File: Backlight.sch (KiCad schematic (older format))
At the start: 52 parts, among them Q2 Q_NMOS_GSD

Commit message: added new generic SMD pad footprints and footprint associations
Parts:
- LED13, LED14, LED15, LED16, LED17, LED18, LED19, LED20, LED21, LED22, LED23, LED24, LED25, LED26, LED27, LED28, LED29, LED30, LED31, LED32, LED33, LED34, LED35, LED36, LED37: footprint (none) -> LED_SMD:LED_0805_2012Metric
- Q2: footprint (none) -> Package_TO_SOT_SMD:SOT-23
- R12, R13, R14, R15, R16, R17, R18, R19, R20, R21, R22, R23, R24, R25, R26, R27, R28, R29, R30, R31, R32, R33, R34, R35, R36: footprint (none) -> Resistor_SMD:R_0805_2012Metric

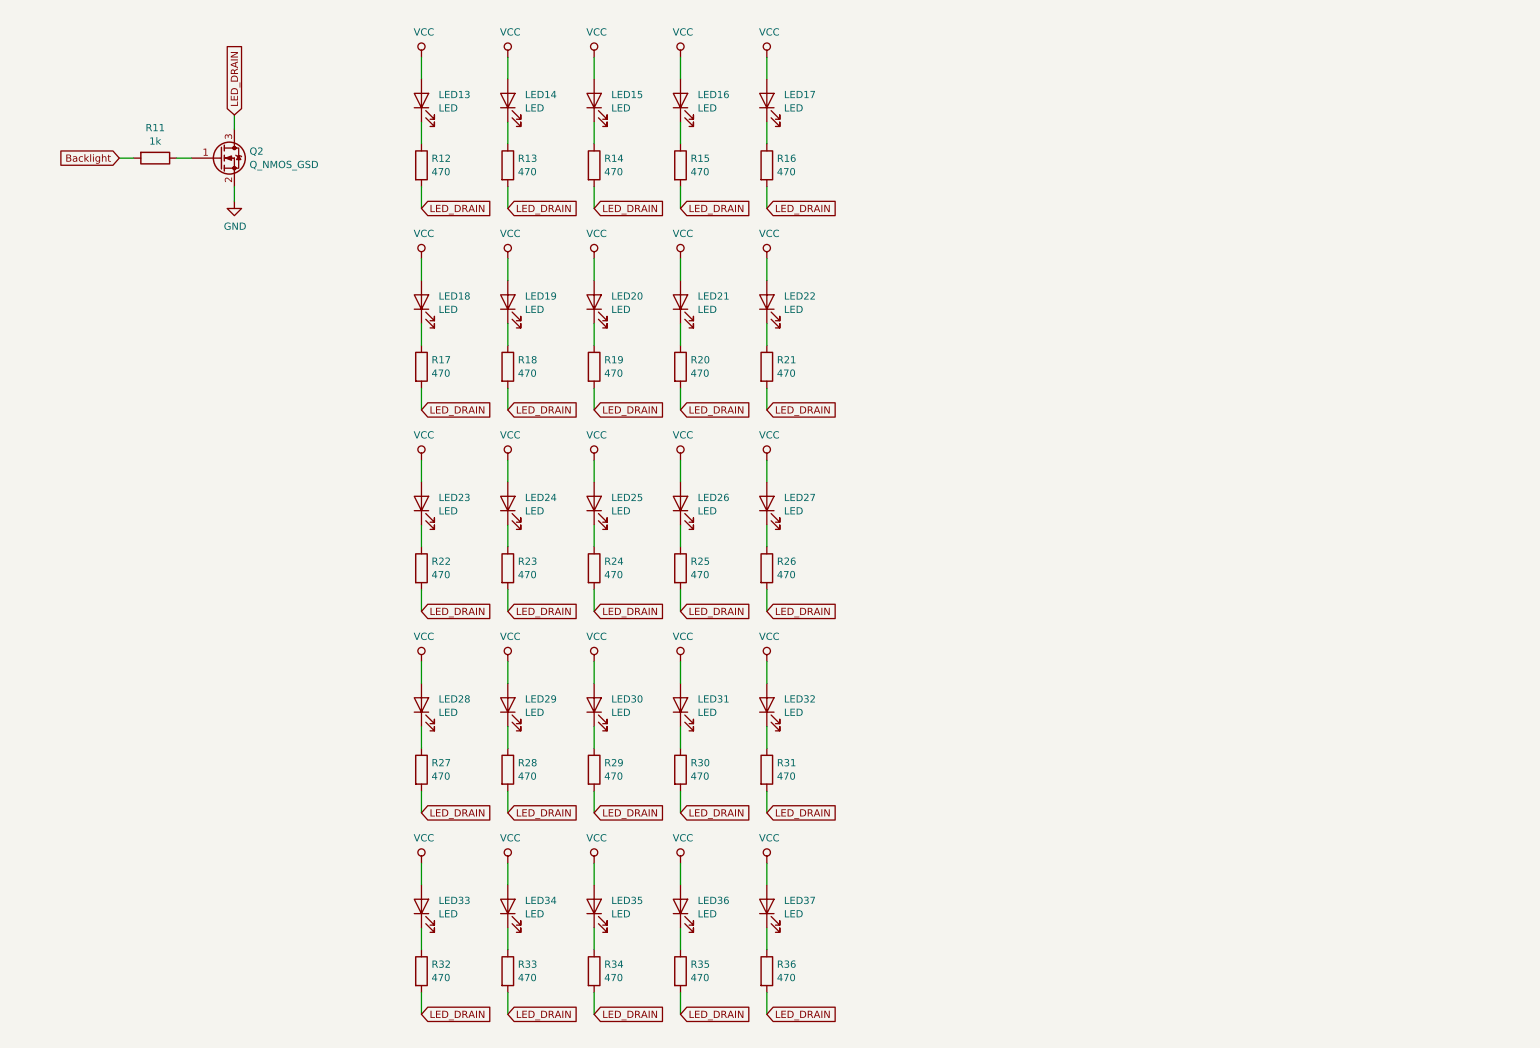
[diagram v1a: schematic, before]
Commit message: updated schematic with more backlight options
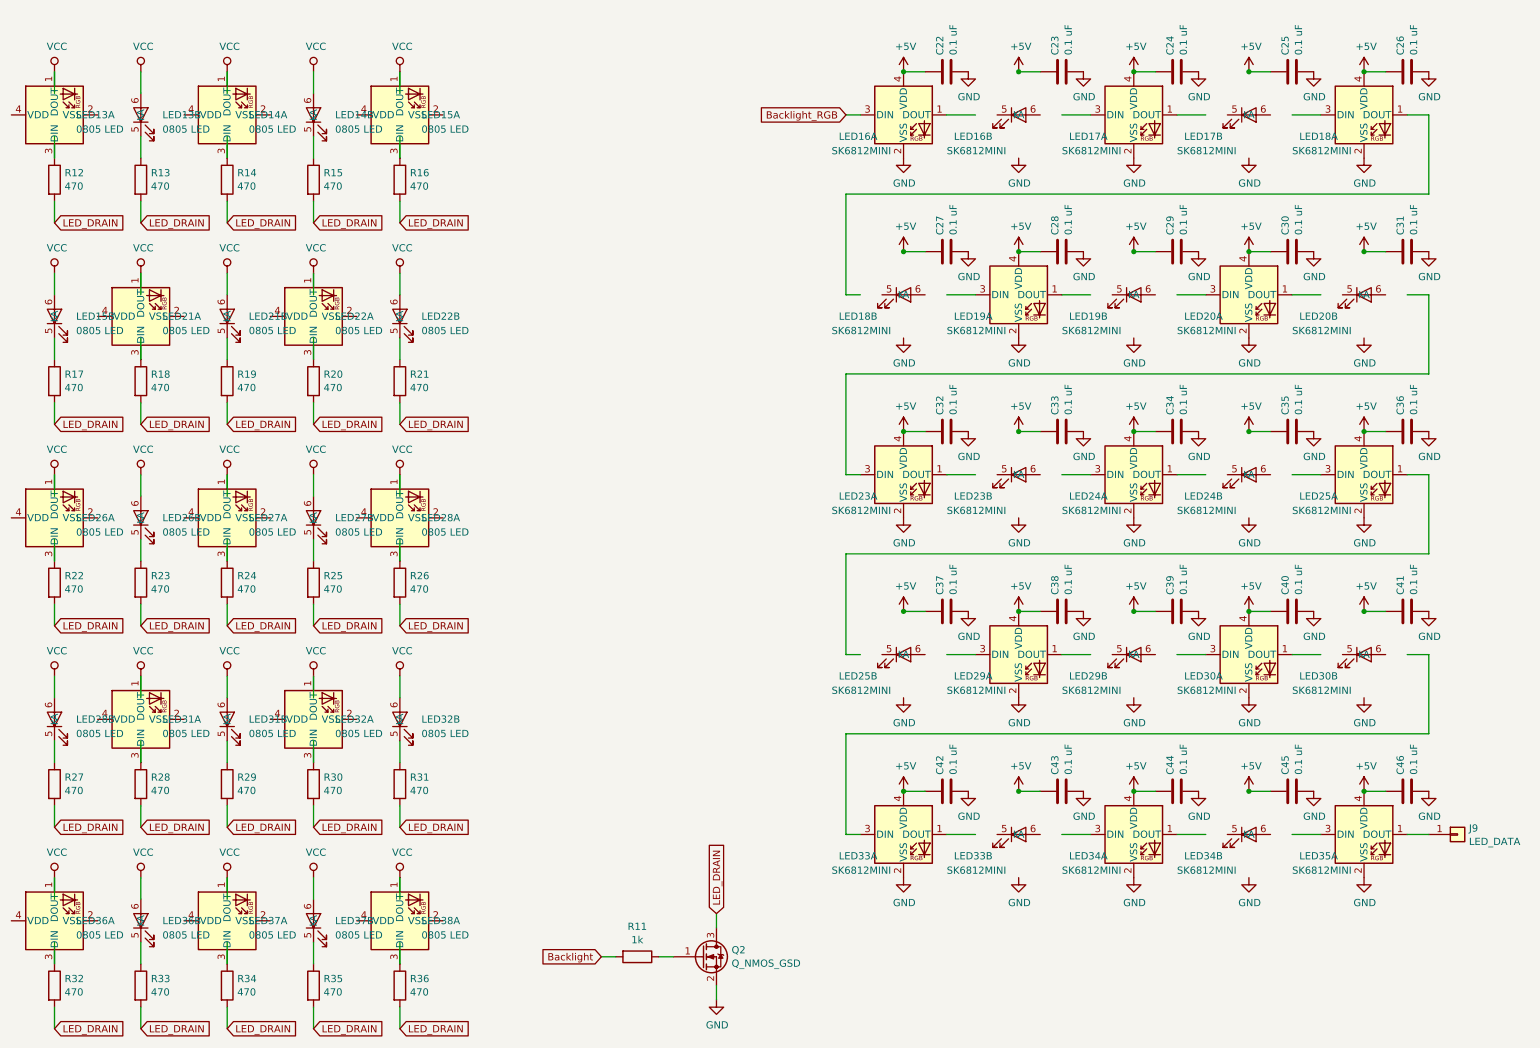
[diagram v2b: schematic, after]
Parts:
- removed LED13, LED14, LED15, LED16, LED17, LED18, LED19, LED20, LED21, LED22, LED23, LED24, LED25, LED26, LED27, LED28, LED29, LED30, LED31, LED32, LED33, LED34, LED35, LED36, LED37: LED, LED_SMD:LED_0805_2012Metric, symbol Device:LED
- added C22, C23, C24, C25, C26, C27, C28, C29, C30, C31, C32, C33, C34, C35, C36, C37, C38, C39, C40, C41, C42, C43, C44, C45, C46: 0.1 uF, Capacitor_SMD:C_0805_2012Metric, symbol Device:C
- added J9: LED_DATA, testatur:Generic_Pads_2mm_1x1, symbol Connector_Generic:Conn_01x01
- added LED13, LED14, LED15, LED21, LED22, LED26, LED27, LED28, LED31, LED32, LED36, LED37, LED38: 0805 LED, testatur:LED_combined_SK6812MINI_0805, symbol testatur:LED_combined_SK6812MINI_0805
- added LED16, LED17, LED18, LED19, LED20, LED23, LED24, LED25, LED29, LED30, LED33, LED34, LED35: SK6812MINI, testatur:LED_combined_SK6812MINI_0805, symbol testatur:LED_combined_SK6812MINI_0805
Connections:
- net labels added: +5V, Backlight_RGB
- wire segments 79 -> 146
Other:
- moved on the sheet: Q2, R11, R12

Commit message: fixed error in the combined LED footprint so symbols arent interchangeable anymore
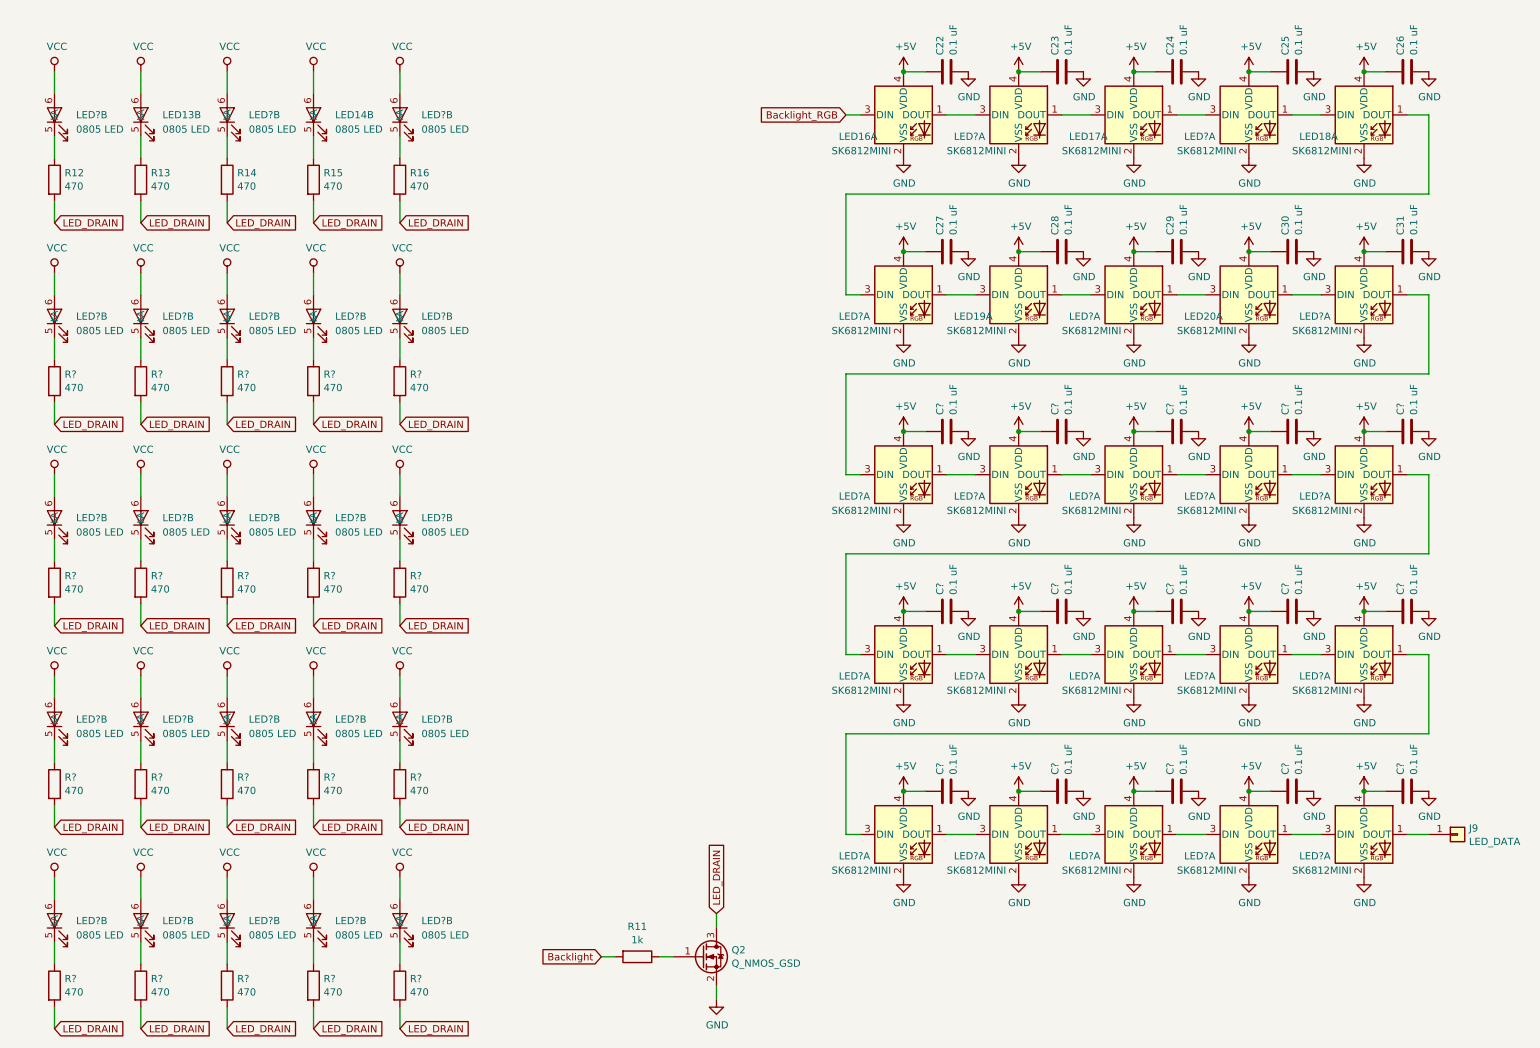
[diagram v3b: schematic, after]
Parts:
- removed C32, C33, C34, C35, C36, C37, C38, C39, C40, C41, C42, C43, C44, C45, C46: 0.1 uF, Capacitor_SMD:C_0805_2012Metric, symbol Device:C
- removed unit 1 of LED13
- removed unit 1 of LED14
- removed LED15, LED21, LED22, LED26, LED27, LED28, LED31, LED32, LED36, LED37, LED38: 0805 LED, testatur:LED_combined_SK6812MINI_0805, symbol testatur:LED_combined_SK6812MINI_0805
- removed unit 2 of LED16
- removed unit 2 of LED17
- removed unit 2 of LED18
- removed unit 2 of LED19
- removed unit 2 of LED20
- removed LED23, LED24, LED25, LED29, LED30, LED33, LED34, LED35: SK6812MINI, testatur:LED_combined_SK6812MINI_0805, symbol testatur:LED_combined_SK6812MINI_0805
- removed R17, R18, R19, R20, R21, R22, R23, R24, R25, R26, R27, R28, R29, R30, R31, R32, R33, R34, R35, R36: 470, Resistor_SMD:R_0805_2012Metric, symbol Device:R
- added C? (x15): 0.1 uF, Capacitor_SMD:C_0805_2012Metric, symbol Device:C
- added LED? (x20): SK6812MINI, testatur:LED_combined_SK6812MINI_0805, symbol testatur:LED_combined_SK6812MINI_0805
- added LED? (x23): 0805 LED, testatur:LED_combined_SK6812MINI_0805, symbol testatur:LED_combined_SK6812MINI_0805
- added R? (x20): 470, Resistor_SMD:R_0805_2012Metric, symbol Device:R

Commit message: new component annotations
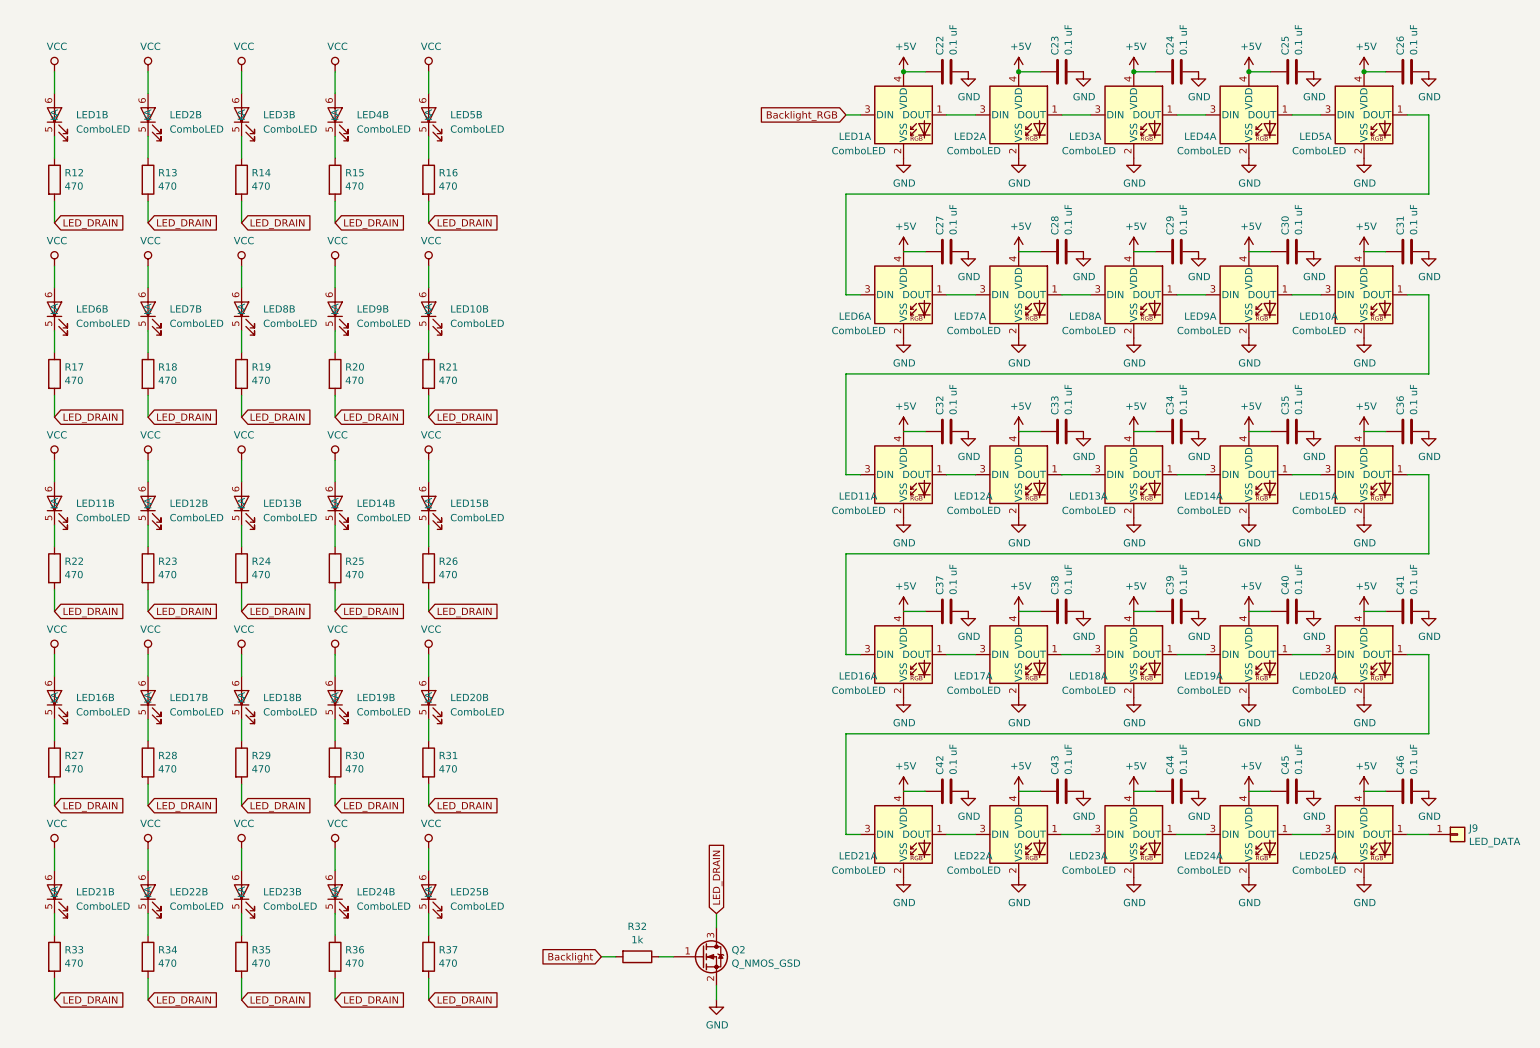
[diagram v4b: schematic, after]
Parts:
- removed C? (x15): 0.1 uF, Capacitor_SMD:C_0805_2012Metric, symbol Device:C
- removed LED? (x20): SK6812MINI, testatur:LED_combined_SK6812MINI_0805, symbol testatur:LED_combined_SK6812MINI_0805
- removed LED? (x20): 0805 LED, testatur:LED_combined_SK6812MINI_0805, symbol testatur:LED_combined_SK6812MINI_0805
- removed R? (x20): 470, Resistor_SMD:R_0805_2012Metric, symbol Device:R
- added C32, C33, C34, C35, C36, C37, C38, C39, C40, C41, C42, C43, C44, C45, C46: 0.1 uF, Capacitor_SMD:C_0805_2012Metric, symbol Device:C
- added LED10, LED11, LED12, LED13, LED14, LED15, LED16, LED21, LED22, LED23, LED24, LED25, LED6, LED7, LED8, LED9: ComboLED, testatur:LED_combined_SK6812MINI_0805, symbol testatur:LED_combined_SK6812MINI_0805
- added unit 2 of LED17
- added unit 2 of LED18
- added unit 2 of LED19
- added unit 1 of LED2
- added unit 2 of LED20
- added unit 1 of LED3
- added unit 1 of LED4
- added unit 1 of LED5
- added R17, R18, R19, R20, R21, R22, R23, R24, R25, R26, R27, R28, R29, R30, R31, R33, R34, R35, R36, R37: 470, Resistor_SMD:R_0805_2012Metric, symbol Device:R
- LED1, LED3, LED5: renamed from LED?; value 0805 LED -> ComboLED
- LED1: renamed from LED16; value SK6812MINI -> ComboLED
- LED17, LED18, LED19, LED20: value SK6812MINI -> ComboLED
- LED2: renamed from LED13; value 0805 LED -> ComboLED
- LED4: renamed from LED14; value 0805 LED -> ComboLED
- renumbered R11 to R32
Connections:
- net +5V: now also C32.1, C33.1, C34.1, C35.1, C36.1, C37.1, C38.1, C39.1, C40.1, C41.1, C42.1, C43.1, C44.1, C45.1, C46.1, LED10.4 (VDD), LED11.4 (VDD), LED12.4 (VDD), LED13.4 (VDD), LED14.4 (VDD), LED15.4 (VDD), LED16.4 (VDD), LED2.4 (VDD), LED21.4 (VDD), LED22.4 (VDD), LED23.4 (VDD), LED24.4 (VDD), LED25.4 (VDD), LED3.4 (VDD), LED4.4 (VDD), LED5.4 (VDD), LED6.4 (VDD), LED7.4 (VDD), LED8.4 (VDD), LED9.4 (VDD)
- net GND: now also C32.2, C33.2, C34.2, C35.2, C36.2, C37.2, C38.2, C39.2, C40.2, C41.2, C42.2, C43.2, C44.2, C45.2, C46.2, LED10.2 (VSS), LED11.2 (VSS), LED12.2 (VSS), LED13.2 (VSS), LED14.2 (VSS), LED15.2 (VSS), LED16.2 (VSS), LED2.2 (VSS), LED21.2 (VSS), LED22.2 (VSS), LED23.2 (VSS), LED24.2 (VSS), LED25.2 (VSS), LED3.2 (VSS), LED4.2 (VSS), LED5.2 (VSS), LED6.2 (VSS), LED7.2 (VSS), LED8.2 (VSS), LED9.2 (VSS)
- net LED_DRAIN: now also R17.2, R18.2, R19.2, R20.2, R21.2, R22.2, R23.2, R24.2, R25.2, R26.2, R27.2, R28.2, R29.2, R30.2, R31.2, R33.2, R34.2, R35.2, R36.2, R37.2
- net VCC: now also LED10.6 (A), LED11.6 (A), LED12.6 (A), LED13.6 (A), LED14.6 (A), LED15.6 (A), LED16.6 (A), LED17.6 (A), LED18.6 (A), LED19.6 (A), LED20.6 (A), LED21.6 (A), LED22.6 (A), LED23.6 (A), LED24.6 (A), LED25.6 (A), LED6.6 (A), LED7.6 (A), LED8.6 (A), LED9.6 (A)
- net at LED17.3 (DIN): now also LED16.1 (DOUT)
- net at LED1.1 (DOUT): now also LED2.3 (DIN)
- net at LED18.3 (DIN): now also LED17.1 (DOUT)
- net at LED19.3 (DIN): now also LED18.1 (DOUT)
- net at LED20.3 (DIN): now also LED19.1 (DOUT)
- net at LED20.1 (DOUT): now also LED21.3 (DIN)
- net at J9.1 (Pin_1): now also LED25.1 (DOUT)
- new net: LED6.5 (K), R17.1
- new net: LED7.5 (K), R18.1
- new net: LED8.5 (K), R19.1
- new net: LED9.5 (K), R20.1
- new net: LED10.5 (K), R21.1
- new net: LED11.5 (K), R22.1
- new net: LED12.5 (K), R23.1
- new net: LED13.5 (K), R24.1
- new net: LED14.5 (K), R25.1
- new net: LED15.5 (K), R26.1
- new net: LED16.5 (K), R27.1
- new net: LED17.5 (K), R28.1
- new net: LED18.5 (K), R29.1
- new net: LED19.5 (K), R30.1
- new net: LED20.5 (K), R31.1
- new net: LED21.5 (K), R33.1
- new net: LED22.5 (K), R34.1
- new net: LED23.5 (K), R35.1
- new net: LED24.5 (K), R36.1
- new net: LED25.5 (K), R37.1
- new net: LED2.1 (DOUT), LED3.3 (DIN)
- new net: LED3.1 (DOUT), LED4.3 (DIN)
- new net: LED4.1 (DOUT), LED5.3 (DIN)
- new net: LED5.1 (DOUT), LED6.3 (DIN)
- new net: LED6.1 (DOUT), LED7.3 (DIN)
- new net: LED7.1 (DOUT), LED8.3 (DIN)
- new net: LED8.1 (DOUT), LED9.3 (DIN)
- new net: LED10.3 (DIN), LED9.1 (DOUT)
- new net: LED10.1 (DOUT), LED11.3 (DIN)
- new net: LED11.1 (DOUT), LED12.3 (DIN)
- new net: LED12.1 (DOUT), LED13.3 (DIN)
- new net: LED13.1 (DOUT), LED14.3 (DIN)
- new net: LED14.1 (DOUT), LED15.3 (DIN)
- new net: LED15.1 (DOUT), LED16.3 (DIN)
- new net: LED21.1 (DOUT), LED22.3 (DIN)
- new net: LED22.1 (DOUT), LED23.3 (DIN)
- new net: LED23.1 (DOUT), LED24.3 (DIN)
- new net: LED24.1 (DOUT), LED25.3 (DIN)
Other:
- moved on the sheet: LED2B, LED3B, LED4B, LED5B, R13, R14, R15, R16

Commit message: fixed power flags
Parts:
- removed unit 1 of LED21
- removed unit 1 of LED22
- removed unit 1 of LED23
- removed unit 1 of LED24
- removed unit 1 of LED25
- added LED39, LED40, LED41, LED42, LED43: ComboLED, testatur:LED_combined_SK6812MINI_0805, symbol testatur:LED_combined_SK6812MINI_0805
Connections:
- net +5V is gone; now on net VCC: C22.1, C23.1, C24.1, C25.1, C26.1, C27.1, C28.1, C29.1, C30.1, C31.1, C32.1, C33.1, C34.1, C35.1, C36.1, C37.1, C38.1, C39.1, C40.1, C41.1, C42.1, C43.1, C44.1, C45.1, C46.1, LED1.4 (VDD), LED10.4 (VDD), LED11.4 (VDD), LED12.4 (VDD), LED13.4 (VDD), LED14.4 (VDD), LED15.4 (VDD), LED16.4 (VDD), LED17.4 (VDD), LED18.4 (VDD), LED19.4 (VDD), LED2.4 (VDD), LED20.4 (VDD), LED3.4 (VDD), LED4.4 (VDD), LED5.4 (VDD), LED6.4 (VDD), LED7.4 (VDD), LED8.4 (VDD), LED9.4 (VDD)
- net GND: now also LED39.2 (VSS), LED40.2 (VSS), LED41.2 (VSS), LED42.2 (VSS), LED43.2 (VSS)
- net VCC: now also LED39.4 (VDD), LED40.4 (VDD), LED41.4 (VDD), LED42.4 (VDD), LED43.4 (VDD)
- net at LED10.1 (DOUT): now also LED39.3 (DIN); no longer LED11.3 (DIN)
- net at LED20.1 (DOUT): now also J9.1 (Pin_1)
- new net: LED39.1 (DOUT), LED40.3 (DIN)
- new net: LED40.1 (DOUT), LED41.3 (DIN)
- new net: LED41.1 (DOUT), LED42.3 (DIN)
- new net: LED42.1 (DOUT), LED43.3 (DIN)
- new net: LED11.3 (DIN), LED43.1 (DOUT)
